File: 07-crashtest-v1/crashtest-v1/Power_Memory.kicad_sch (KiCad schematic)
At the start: 0 parts

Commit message: started power
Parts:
- added J1: USB_C_Receptacle_USB2.0_16P, symbol Connector:USB_C_Receptacle_USB2.0_16P
- added U13: USBLC6-2SC6, Package_TO_SOT_SMD:SOT-23-6, symbol Power_Protection:USBLC6-2SC6
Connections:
- new net: J1.A7 (D-), J1.B7 (D-), U13.1 (I/O1)
- new net: J1.A6 (D+), J1.B6 (D+), U13.3 (I/O2)
- new net CC1: J1.A5 (CC1)
- new net CC2: J1.B5 (CC2)
- new net GND: J1.A1 (GND), J1.A12 (GND), J1.B1 (GND), J1.B12 (GND), J1.SH (SHIELD), U13.2 (GND)
- new net USB_D_N: U13.6 (I/O1)
- new net USB_D_P: U13.4 (I/O2)
- new net VBUS: J1.A4 (VBUS), J1.A9 (VBUS), J1.B4 (VBUS), J1.B9 (VBUS)
- no-connect marks 0 -> 2

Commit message: buck converter
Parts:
- added C13: 100uF, symbol Device:C_Small_US
- added C14: 470pF, symbol Device:C_Small
- added C15: 47uF, symbol Device:C_Small_US
- added C16: 10uF, symbol Device:C_Small
- added D1: DSS14U, symbol Device:D_Schottky
- added L1: 220uH, symbol Device:L_Small
- added L2: 10uH, symbol Device:L_Small
- added R1: 330m, symbol Device:R_Small_US
- added R2: 1.8k, symbol Device:R_Small_US
- added R3: 1.1k, symbol Device:R_Small_US
- added U1: AZ34063UMTR-G1, SO-8_AZ3406-M_DIO, symbol CrashtestSymbols:AZ34063UMTR-G1
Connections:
- net GND: now also C13.2, C14.2, C15.2, C16.2, D1.2 (A), R3.2, U1.4 (GND)
- new net: C15.1, L1.1, L2.2, R2.1
- new net: R2.2, R3.1, U1.5 (COMPARATORINVERTINGINPUT)
- new net: D1.1 (K), L1.2, U1.2 (SWITCHEMITTER)
- new net: R1.1, U1.1 (SWITCHCOLLECTOR), U1.7 (IPKSENSE), U1.8 (DRIVERCOLLECTOR)
- new net: C14.1, U1.3 (TIMINGCAPACITOR)
- new net 3V3: C16.1, L2.1
- new net VBAT: C13.1, R1.2, U1.6 (VCC)
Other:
- note added: "Vout = 1.25 (R2+R3)/R3 R2/R3 = 1.64 = 1.8/1.1"

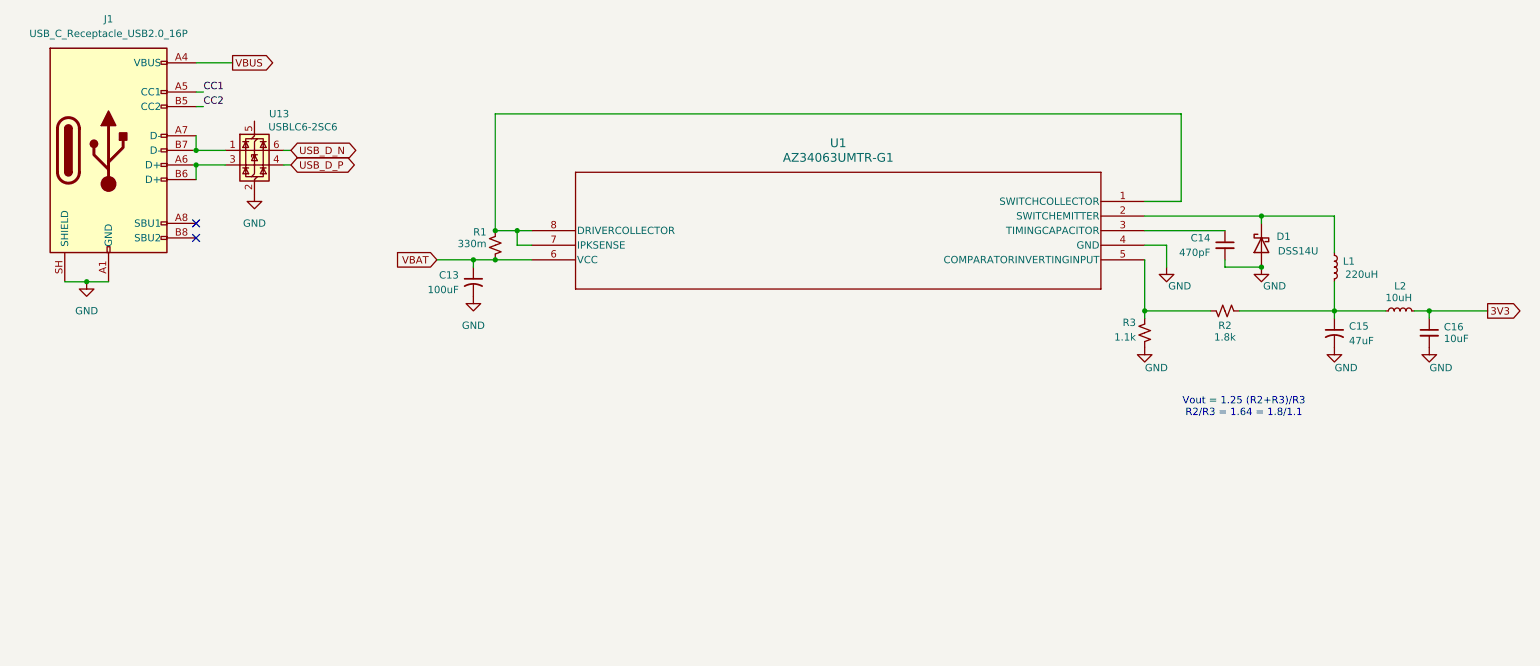
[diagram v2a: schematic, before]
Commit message: completed basic power management
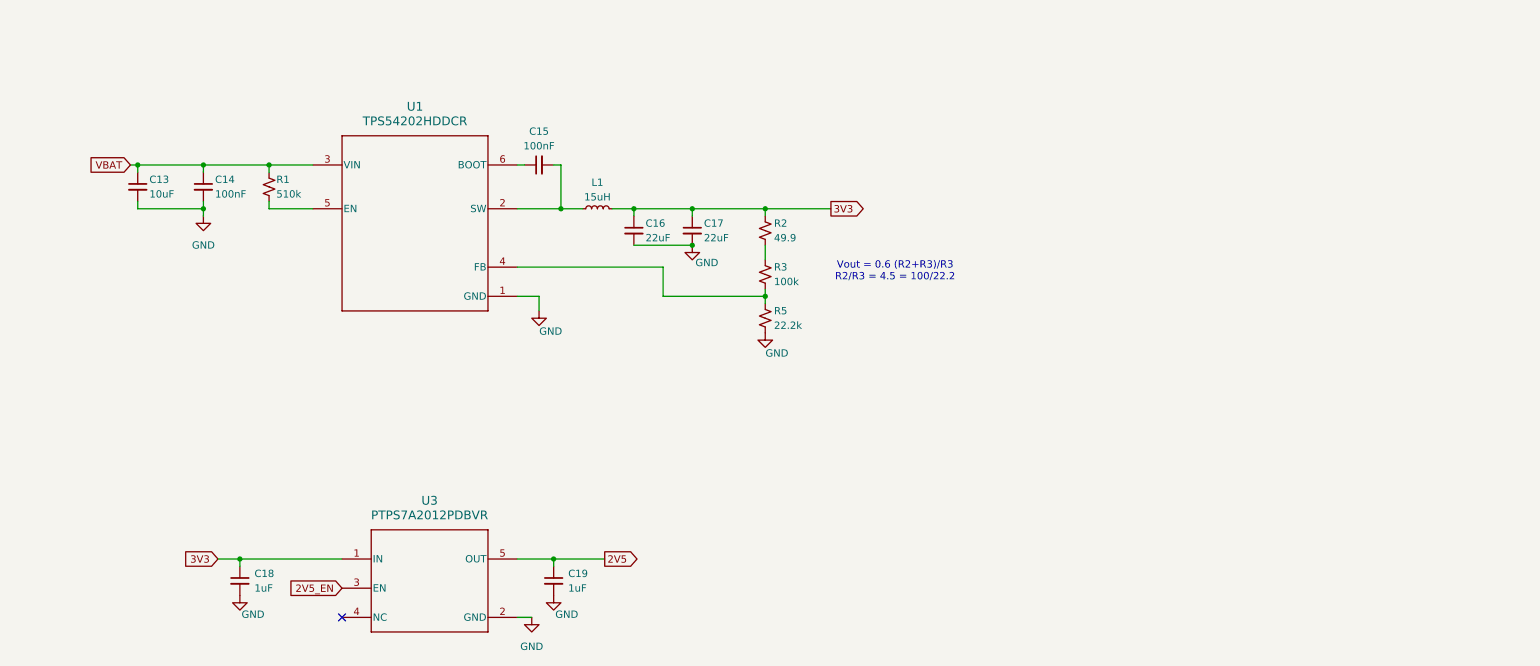
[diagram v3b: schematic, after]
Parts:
- removed C13: 100uF, symbol Device:C_Small_US
- removed C15: 47uF, symbol Device:C_Small_US
- removed D1: DSS14U, symbol Device:D_Schottky
- removed J1: USB_C_Receptacle_USB2.0_16P, symbol Connector:USB_C_Receptacle_USB2.0_16P
- removed L2: 10uH, symbol Device:L_Small
- removed U1: AZ34063UMTR-G1, SO-8_AZ3406-M_DIO, symbol CrashtestSymbols:AZ34063UMTR-G1
- removed U13: USBLC6-2SC6, Package_TO_SOT_SMD:SOT-23-6, symbol Power_Protection:USBLC6-2SC6
- added C13: 10uF, symbol Device:C_Small
- added C15: 100nF, symbol Device:C_Small
- added C17: 22uF, symbol Device:C_Small
- added C18, C19: 1uF, symbol Device:C_Small
- added R5: 22.2k, symbol Device:R_Small_US
- added U1: TPS54202HDDCR, DDC0006A_N, symbol CrashtestSymbols:TPS54202HDDCR
- added U3: PTPS7A2012PDBVR, DBV0005A-IPC_A, symbol CrashtestSymbols:PTPS7A2012PDBVR
- C14: value 470pF -> 100nF
- C16: value 10uF -> 22uF
- L1: value 220uH -> 15uH
- R1: value 330m -> 510k
- R2: value 1.8k -> 49.9
- R3: value 1.1k -> 100k
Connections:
- net 3V3: now also L1.2, R2.1, C17.1, C18.1, U3.1 (IN)
- net GND: now also C13.2, C17.2, C18.2, C19.2, R5.2, U1.1 (GND), U3.2 (GND); no longer R3.2
- net VBAT: now also C14.1, R1.1, C13.1, U1.3 (VIN); no longer R1.2
- net at L1.1: now also C15.2, U1.2 (SW); no longer R2.1
- new net: R3.2, R5.1, U1.4 (FB)
- new net: R1.2, U1.5 (EN)
- new net: C15.1, U1.6 (BOOT)
- new net 2V5: C19.1, U3.5 (OUT)
- new net 2V5_EN: U3.3 (EN)
- no-connect marks 2 -> 1
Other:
- note added: "Vout = 0.6 (R2+R3)/R3 R2/R3 = 4.5 = 100/22.2"
- note removed: "Vout = 1.25 (R2+R3)/R3 R2/R3 = 1.64 = 1.8/1.1"
